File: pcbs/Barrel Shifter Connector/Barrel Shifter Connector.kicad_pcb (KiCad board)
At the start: 2 copper layers, 72.4 x 127 mm, 8 parts, among them J103 Conn_02x20_Odd_Even, J104 Conn_02x20_Odd_Even, J105 Conn_01x04, Q101 2N3904

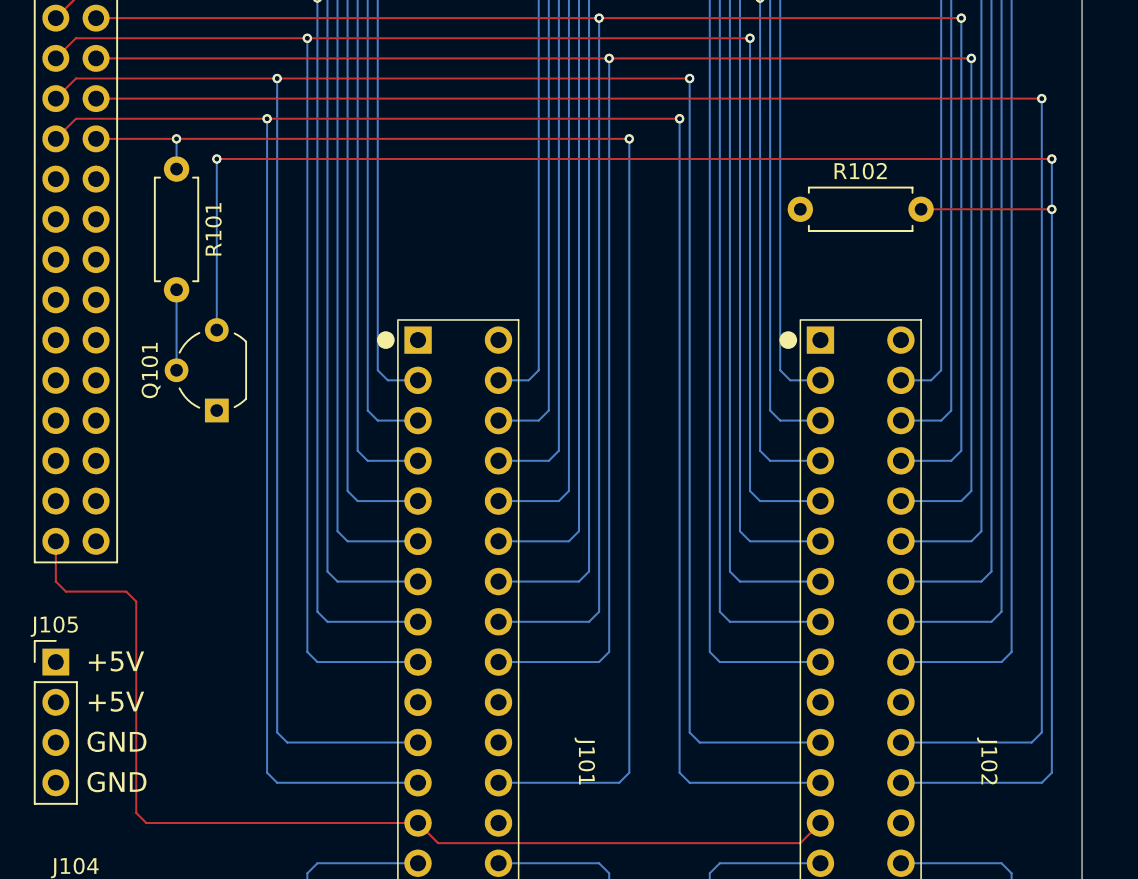
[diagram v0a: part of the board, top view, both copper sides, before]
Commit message: Missing wire
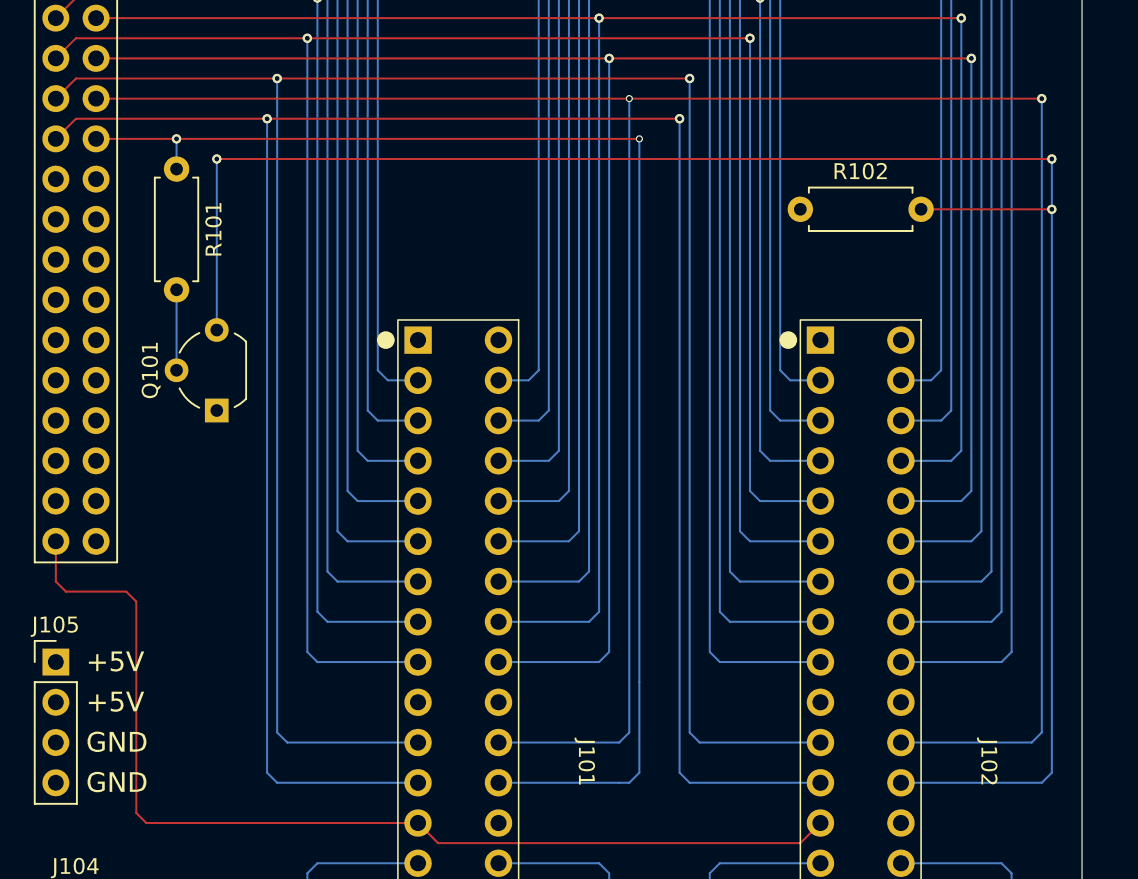
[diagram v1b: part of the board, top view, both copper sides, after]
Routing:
- net /B_1: track 108.8 -> 157.4 mm, vias 1 -> 2
- net /B_3: track 84.1 -> 85.4 mm
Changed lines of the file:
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@@
 	(segment
 		(start 111.76 71.12)
+		(end 145.415 71.12)
+		(width 0.127)
+		(layer "F.Cu")
+		(net 4)
+	)
+	(segment
+		(start 145.415 71.12)
 		(end 171.45 71.12)
 		(width 0.127)
@@
 		(drill 0.3)
 		(layers "F.Cu" "B.Cu")
+		(net 4)
+	)
+	(via
+		(at 145.415 71.12)
+		(size 0.45)
+		(drill 0.3)
+		(layers "F.Cu" "B.Cu")
+		(net 4)
+	)
+	(segment
+		(start 145.415 111.125)
+		(end 145.415 71.12)
+		(width 0.127)
+		(layer "B.Cu")
+		(net 4)
+	)
+	(segment
+		(start 137.16 111.76)
+		(end 144.78 111.76)
+		(width 0.127)
+		(layer "B.Cu")
 		(net 4)
 	)
@@
 	)
 	(segment
+		(start 144.78 111.76)
+		(end 145.415 111.125)
+		(width 0.127)
+		(layer "B.Cu")
+		(net 4)
+	)
+	(segment
 		(start 162.56 111.76)
 		(end 170.815 111.76)
@@
 	)
 	(segment
-		(start 116.84 73.66)
-		(end 145.415 73.66)
-		(width 0.127)
-		(layer "F.Cu")
-		(net 14)
-	)
-	(via
-		(at 145.415 73.66)
-		(size 0.6)
+		(start 146.05 73.66)
+		(end 116.84 73.66)
+		(width 0.127)
+		(layer "F.Cu")
+		(net 14)
+	)
+	(via
+		(at 146.05 73.66)
+		(size 0.45)
 		(drill 0.3)
 		(layers "F.Cu" "B.Cu")
@@
 	)
 	(segment
-		(start 145.415 113.665)
-		(end 145.415 73.66)
+		(start 146.05 113.665)
+		(end 146.05 107.95)
 		(width 0.127)
 		(layer "B.Cu")
@@
 	)
 	(segment
+		(start 146.05 107.95)
+		(end 146.05 73.66)
+		(width 0.127)
+		(layer "B.Cu")
+		(net 14)
+	)
+	(segment
 		(start 144.78 114.3)
-		(end 145.415 113.665)
-		(width 0.127)
-		(layer "B.Cu")
+		(end 145.415 114.3)
+		(width 0.127)
+		(layer "B.Cu")
+		(net 14)
+	)
+	(segment
+		(start 145.415 114.3)
+		(end 146.05 113.665)
+		(width 0.127)
+		(layer "B.Cu")
